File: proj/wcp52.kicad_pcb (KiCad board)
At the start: 4 copper layers, 100 x 100 mm, 301 parts, among them J1 MicroUSB-B, J2 IN1, J3 IN2, J4 OUT, J5 CONN-PJ-037A, J6 JLINK, J7 AUX, Q1 MMBT3906, Q10 MMBT3904, Q11 BFR540, Q12 BFR540, Q13 MMBT3904, Q14 MMBT3904, Q15 MMBT3904, Q16 MMBT3904, Q17 PZT2907A, Q18 PZT2907A, Q19 MMBT3904, Q2 IRLML6402, Q3 AOD417, Q4 MMBT3906, Q5 2N7002, Q6 2N7002, Q7 MMBT3906, Q8 2N7002, Q9 2N7002, U1 TL431AIDBZ, U10 MASWSS0162, U11 AD8310ARMZ, U12 ATSAM4S16CA-AU, U13 FT230XS_DNP, U14 L78M05CDT, U15 MC79M05CDT, U16 AZ1117CH-1.8TRG1, U17 MCP1700T-vv02E/TT, U2 LM393M, U3 LMH6714MF, U4 AD9958BCPZ, U5 LMH6714MF, U6 AD8000YRDZ, U7 THS3001IDGN, U8 MAADSS0008, U9 MASWSS0162, X1 25 MHz, X2 12MHz

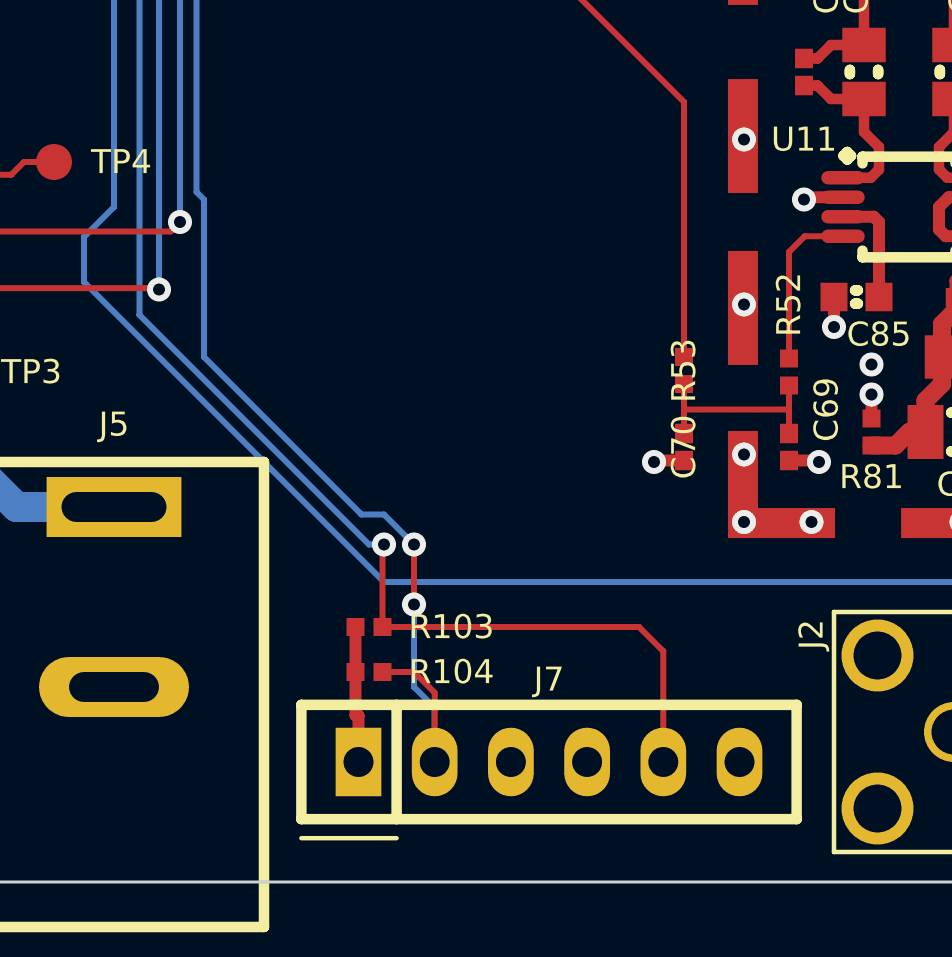
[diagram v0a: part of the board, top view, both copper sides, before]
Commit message: Add overload protection to aux power output
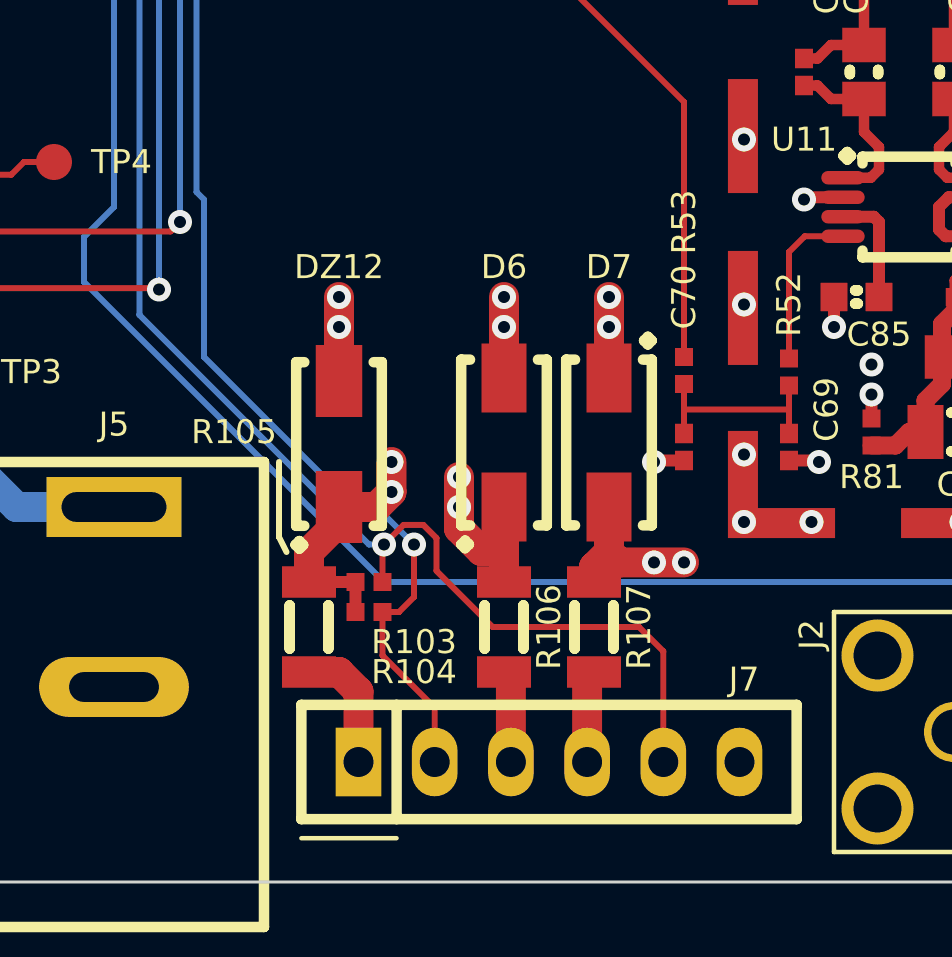
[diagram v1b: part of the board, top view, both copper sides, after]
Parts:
- added D6: S1A, IPC7351-Nominal:DIOM5326X292, F.Cu at (113.0, 110.3)
- added D7: S1A, IPC7351-Nominal:DIOM5326X292, F.Cu at (116.5, 110.3)
- added DZ12: 1SMA5914BT3G, IPC7351-Nominal:DIOM5226X203, F.Cu at (107.5, 110.4)
- added R105: 50mA, IPC7351-Nominal:RESC3216X60, F.Cu at (106.5, 116.5)
- added R106: 50mA, IPC7351-Nominal:RESC3216X60, F.Cu at (113.0, 116.5)
- added R107: 50mA, IPC7351-Nominal:RESC3216X60, F.Cu at (116.0, 116.5)
- moved R104 2.00 mm to (108.5, 116.0)
- moved R103 1.50 mm to (108.5, 115.0)
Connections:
- J7 pad 1: +3.3 -> Net-(J7-Pad1)
- J7 pad 3: +9 -> Net-(J7-Pad3)
- J7 pad 4: -9 -> Net-(J7-Pad4)
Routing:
- net GND: track 614.5 -> 622.7 mm, vias 241 -> 247
- net Net-(J7-Pad1): track 0.00 -> 4.27 mm
- net +3.3: track 112.8 -> 116.7 mm, vias 10 -> 12
- net +9: track 218.2 -> 222.1 mm, vias 8 -> 10
- net Net-(J7-Pad4): track 0.00 -> 3.48 mm
- net /MPU/I2C_SCL: track 61.1 -> 58.0 mm, vias 3 -> 2
- net Net-(J7-Pad3): track 0.00 -> 3.10 mm
- net /MPU/I2C_SDA: track 65.7 -> 66.4 mm
- net -9: track 276.4 -> 276.8 mm, vias 16 -> 18

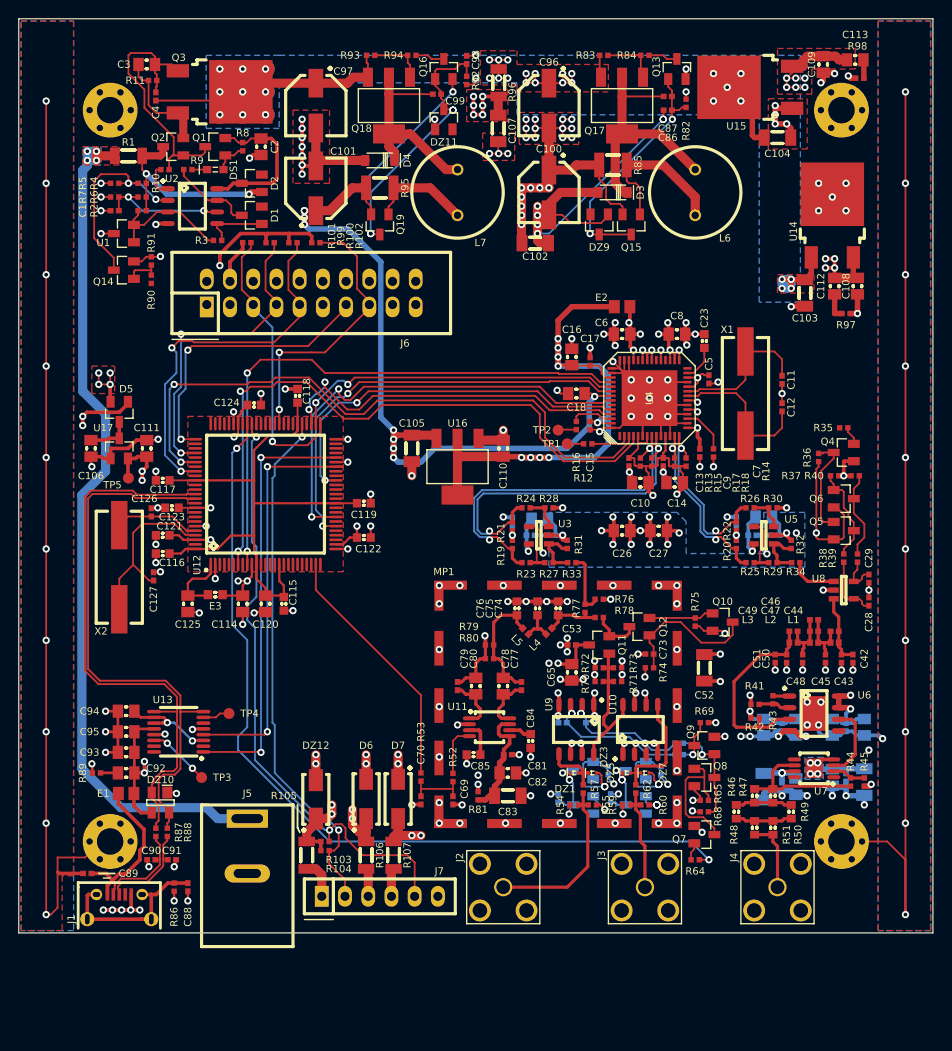
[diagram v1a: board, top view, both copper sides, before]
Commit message: Add some test points
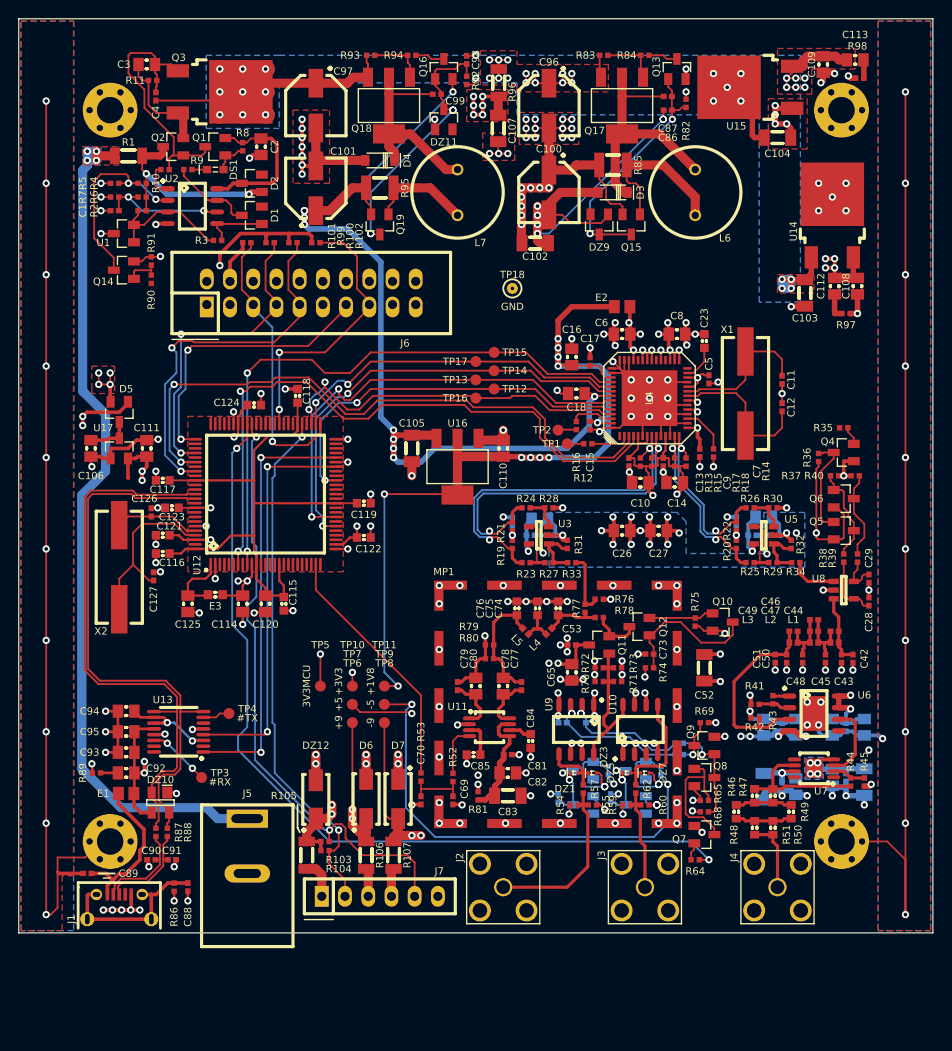
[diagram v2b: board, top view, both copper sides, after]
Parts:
- added TP10: +3V3, conn-test:TEST-SMD-SMALL, F.Cu at (111.5, 98.0)
- added TP11: +1V8, conn-test:TEST-SMD-SMALL, F.Cu at (115.0, 98.0)
- added TP12: MISO, conn-test:TEST-SMD-SMALL, F.Cu at (127.0, 65.5)
- added TP13: MOSI, conn-test:TEST-SMD-SMALL, F.Cu at (125.0, 64.5)
- added TP14: SCK, conn-test:TEST-SMD-SMALL, F.Cu at (127.0, 63.5)
- added TP15: IOUP, conn-test:TEST-SMD-SMALL, F.Cu at (127.0, 61.5)
- added TP16: SYNC, conn-test:TEST-SMD-SMALL, F.Cu at (125.0, 66.5)
- added TP17: #CS, conn-test:TEST-SMD-SMALL, F.Cu at (125.0, 62.5)
- added TP18: GND, conn-test:TEST-SMD-SMALL, F.Cu at (129.0, 54.5)
- added TP6: +9, conn-test:TEST-SMD-SMALL, F.Cu at (111.5, 102.0)
- added TP7: +5, conn-test:TEST-SMD-SMALL, F.Cu at (111.5, 100.0)
- added TP8: -9, conn-test:TEST-SMD-SMALL, F.Cu at (115.0, 102.0)
- added TP9: -5, conn-test:TEST-SMD-SMALL, F.Cu at (115.0, 100.0)
- moved TP5 31.0 mm to (108.0, 98.0)
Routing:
- net -5: track 215.6 -> 265.0 mm, vias 24 -> 25
- net +1.8: track 65.3 -> 96.4 mm, vias 9 -> 11
- net -9: track 276.8 -> 288.6 mm
- net +9: track 222.1 -> 231.6 mm
- net +5: track 277.8 -> 287.3 mm, vias 21 -> 22
- net +3.3SB: track 46.8 -> 50.3 mm, vias 10 -> 11
- net /Synth/IO_UPDATE: track 62.4 -> 64.3 mm
- net +3.3: track 116.7 -> 118.2 mm, vias 12 -> 13
- net /Synth/#CS: track 36.5 -> 38.0 mm
- net /Synth/SCLK: track 48.0 -> 49.0 mm
- net /Synth/SDI: track 50.0 -> 50.6 mm

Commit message: Tidy up F.Cu
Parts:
- added TP19: LEVEL, conn-test:TEST-SMD-SMALL, F.Cu at (115.0, 96.0)
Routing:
- net Net-(C127-Pad2): track 19.8 -> 22.8 mm
- net /Comm/USBPWR: track 21.7 -> 24.2 mm, vias 4 -> 6
- net -9: track 288.6 -> 290.2 mm
- net /MPU/ADIN: track 27.6 -> 29.2 mm
- net Net-(R2-Pad2): track 14.3 -> 15.6 mm
- net Net-(D1-Pad3): track 9.30 -> 10.5 mm
- net /Synth/IO_UPDATE: track 64.3 -> 63.1 mm
- net /MPU/TMS: track 34.8 -> 35.8 mm
- net /MPU/TDO: track 31.4 -> 32.3 mm
- net /MPU/#RST: track 30.5 -> 31.4 mm
- net /Synth/PWR_DWN_CTL: track 70.3 -> 69.6 mm
- net /Synth/MASTER_RESET: track 68.2 -> 67.7 mm
- added copper zone on F.Cu, net +1.8A
- added copper zone on F.Cu, net +3.3
- added copper zone on F.Cu, net /Comm/USBPWR

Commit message: Tidy up In1.Cu
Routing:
- net +5: track 287.3 -> 290.5 mm
- net +9: track 231.6 -> 230.4 mm
- net -9: track 290.2 -> 289.2 mm
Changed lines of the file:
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@@
     (thickness 1.6)
     (drawings 18)
-    (tracks 2882)
+    (tracks 2878)
     (zones 0)
     (modules 321)
@@
   (page A4)
   (layers
-    (0 F.Cu signal)
-    (1 In1.Cu signal hide)
+    (0 F.Cu signal hide)
+    (1 In1.Cu signal)
     (2 In2.Cu signal hide)
     (31 B.Cu signal hide)
@@
     (34 B.Paste user)
     (35 F.Paste user)
-    (36 B.SilkS user)
+    (36 B.SilkS user hide)
     (37 F.SilkS user hide)
     (38 B.Mask user)
     (39 F.Mask user)
-    (40 Dwgs.User user)
+    (40 Dwgs.User user hide)
     (41 Cmts.User user)
     (42 Eco1.User user)
@@
   )
   (setup
-    (last_trace_width 0.2)
+    (last_trace_width 1)
     (trace_clearance 0.152)
     (zone_clearance 0.2)
@@
     (mod_text_size 1 1)
     (mod_text_width 0.15)
-    (pad_size 1.2 1.2)
-    (pad_drill 0.4)
+    (pad_size 2 5)
+    (pad_drill 1)
     (pad_to_mask_clearance 0)
     (aux_axis_origin 0 0)
-    (visible_elements FFFE7F7F)
+    (visible_elements FFFC3E7F)
     (pcbplotparams
       (layerselection 0x00030_80000001)
@@
       (net 79 /PowerInput/IN))
     (pad 2 thru_hole oval (at 0 0 270) (size 2 5) (drill oval 1 3) (layers *.Cu *.Mask F.SilkS)
-      (net 1 GND))
+      (net 1 GND) (thermal_width 1.5))
     (model conn_misc/dc_socket.wrl
       (at (xyz 0 0 0))
@@
   (via (at 109.25 111) (size 0.8) (drill 0.4) (layers F.Cu B.Cu) (net 11))
   (segment (start 109.25 112) (end 109.25 111) (width 1) (layer F.Cu) (net 11))
+  (segment (start 85 63.75) (end 85 52) (width 0.2) (layer In1.Cu) (net 12))
+  (segment (start 85 52) (end 87 50) (width 0.2) (layer In1.Cu) (net 12))
+  (segment (start 87 50) (end 151.5 50) (width 0.2) (layer In1.Cu) (net 12))
+  (segment (start 151.5 50) (end 156.050001 54.550001) (width 0.2) (layer In1.Cu) (net 12))
+  (segment (start 156.050001 54.550001) (end 157.699999 54.550001) (width 0.2) (layer In1.Cu) (net 12))
   (segment (start 118 101) (end 120.5 101) (width 0.2) (layer In1.Cu) (net 12))
   (segment (start 111.5 100) (end 112.352001 100.852001) (width 0.2) (layer F.Cu) (net 12))
@@
   (segment (start 85 65) (end 85 66.85) (width 0.4) (layer F.Cu) (net 12))
   (segment (start 85 66.85) (end 85.05 66.9) (width 0.4) (layer F.Cu) (net 12))
-  (segment (start 85 63.75) (end 85 57.464962) (width 0.2) (layer In1.Cu) (net 12))
-  (segment (start 85 57.464962) (end 92.464962 50) (width 0.2) (layer In1.Cu) (net 12))
-  (segment (start 92.464962 50) (end 151.5 50) (width 0.2) (layer In1.Cu) (net 12))
-  (segment (start 151.5 50) (end 156.050001 54.550001) (width 0.2) (layer In1.Cu) (net 12))
-  (segment (start 156.050001 54.550001) (end 157.699999 54.550001) (width 0.2) (layer In1.Cu) (net 12))
   (segment (start 83.75 65) (end 83.75 63.75) (width 0.2) (layer F.Cu) (net 12))
   (via (at 83.75 63.75) (size 0.8) (drill 0.4) (layers F.Cu B.Cu) (net 12))
@@
   (segment (start 166.95 86.55) (end 166.35 86.55) (width 0.2) (layer F.Cu) (net 16))
   (segment (start 167.25 86.25) (end 166.95 86.55) (width 0.2) (layer F.Cu) (net 16))
+  (segment (start 173.5 104.5) (end 170.916189 107.083811) (width 1) (layer In1.Cu) (net 17))
+  (segment (start 163.584648 108.8) (end 158.48108 108.8) (width 1) (layer In1.Cu) (net 17))
+  (segment (start 170.916189 107.083811) (end 165.300837 107.083811) (width 1) (layer In1.Cu) (net 17))
+  (segment (start 165.300837 107.083811) (end 163.584648 108.8) (width 1) (layer In1.Cu) (net 17))
   (segment (start 111.5 102) (end 111.5 111.5) (width 0.2) (layer F.Cu) (net 17))
   (via (at 158.5 107.5) (size 0.8) (drill 0.4) (layers F.Cu B.Cu) (net 17))
@@
   (segment (start 158.5 107.5) (end 159.4 107.5) (width 0.6) (layer B.Cu) (net 17))
   (segment (start 158.5 108.55) (end 158.5 107.5) (width 0.6) (layer B.Cu) (net 17))
-  (segment (start 170.5 108.056962) (end 168.754961 109.802001) (width 1) (layer In1.Cu) (net 17))
-  (segment (start 170.5 107.5) (end 170.5 108.056962) (width 1) (layer In1.Cu) (net 17))
-  (segment (start 173.5 104.5) (end 170.5 107.5) (width 1) (layer In1.Cu) (net 17))
   (segment (start 170.75 89) (end 173.5 91.75) (width 1) (layer In1.Cu) (net 17))
   (segment (start 170.75 86.039302) (end 170.75 89) (width 1) (layer In1.Cu) (net 17))
@@
   (segment (start 166.350001 63.149999) (end 166.350001 81.639303) (width 1) (layer In1.Cu) (net 17))
   (segment (start 170.75 58.75) (end 166.350001 63.149999) (width 1) (layer In1.Cu) (net 17))
-  (segment (start 168.754961 109.802001) (end 166.858963 109.802001) (width 1) (layer In1.Cu) (net 17))
   (segment (start 170.75 29.75) (end 170.75 58.75) (width 1) (layer In1.Cu) (net 17))
   (segment (start 168 27) (end 170.75 29.75) (width 1) (layer In1.Cu) (net 17))
@@
   (segment (start 146.5 27) (end 168 27) (width 1) (layer In1.Cu) (net 17))
   (segment (start 140 33.5) (end 146.5 27) (width 1) (layer In1.Cu) (net 17))
-  (segment (start 166.858963 109.802001) (end 165.856962 108.8) (width 1) (layer In1.Cu) (net 17))
   (segment (start 125.75 33.5) (end 140 33.5) (width 1) (layer In1.Cu) (net 17))
   (segment (start 149.556968 115.75) (end 148.39982 115.75) (width 1) (layer In1.Cu) (net 17))
@@
   (segment (start 158.5 107.5) (end 158.5 108.78108) (width 1) (layer In1.Cu) (net 17))
   (segment (start 158.48108 108.8) (end 156.506968 108.8) (width 1) (layer In1.Cu) (net 17))
-  (segment (start 165.856962 108.8) (end 158.48108 108.8) (width 1) (layer In1.Cu) (net 17))
   (segment (start 123.42175 117.110248) (end 118.610248 117.110248) (width 1) (layer In1.Cu) (net 17))
   (segment (start 124.781998 115.75) (end 123.42175 117.110248) (width 0.4) (layer In1.Cu) (net 17))
@@
   (segment (start 112.246133 113.967669) (end 111.5 113.221536) (width 1) (layer F.Cu) (net 17))
   (segment (start 113 113.967669) (end 112.246133 113.967669) (width 1) (layer F.Cu) (net 17))
+  (segment (start 152.069541 33.680459) (end 157 28.75) (width 1) (layer In1.Cu) (net 18))
+  (segment (start 166.75 28.75) (end 169.5 31.5) (width 1) (layer In1.Cu) (net 18))
+  (segment (start 157 28.75) (end 166.75 28.75) (width 1) (layer In1.Cu) (net 18))
+  (segment (start 169.5 31.5) (end 169.5 57.5) (width 1) (layer In1.Cu) (net 18))
+  (segment (start 169.5 57.5) (end 164 63) (width 1) (layer In1.Cu) (net 18))
+  (segment (start 170 105) (end 168 105) (width 1) (layer In1.Cu) (net 18))
+  (segment (start 164 63) (end 164 81.477932) (width 1) (layer In1.Cu) (net 18))
+  (segment (start 164 81.477932) (end 169.5 86.977932) (width 1) (layer In1.Cu) (net 18))
+  (segment (start 169.5 86.977932) (end 169.5 90) (width 1) (layer In1.Cu) (net 18))
+  (segment (start 169.5 90) (end 170.75 91.25) (width 1) (layer In1.Cu) (net 18))
+  (segment (start 170.75 91.25) (end 170.75 104.25) (width 1) (layer In1.Cu) (net 18))
+  (segment (start 170.75 104.25) (end 170 105) (width 1) (layer In1.Cu) (net 18))
   (segment (start 131.75 45.5) (end 132.05 45.5) (width 1) (layer F.Cu) (net 18))
   (segment (start 132.05 45.5) (end 133 46.45) (width 1) (layer F.Cu) (net 18))
@@
   (segment (start 149.350001 112.899999) (end 148.610027 112.899999) (width 1) (layer In1.Cu) (net 18))
   (segment (start 162.4 105) (end 157.25 105) (width 1) (layer In1.Cu) (net 18))
-  (segment (start 152.069541 33.680459) (end 157 28.75) (width 1) (layer In1.Cu) (net 18))
-  (segment (start 157 28.75) (end 166.75 28.75) (width 1) (layer In1.Cu) (net 18))
-  (segment (start 166.75 28.75) (end 169.5 31.5) (width 1) (layer In1.Cu) (net 18))
-  (segment (start 169.5 31.5) (end 169.5 57.5) (width 1) (layer In1.Cu) (net 18))
-  (segment (start 169.5 57.5) (end 164 63) (width 1) (layer In1.Cu) (net 18))
-  (segment (start 164 63) (end 164 83.25) (width 1) (layer In1.Cu) (net 18))
-  (segment (start 164 83.25) (end 166.75 86) (width 1) (layer In1.Cu) (net 18))
-  (segment (start 166.75 86) (end 168.522068 86) (width 1) (layer In1.Cu) (net 18))
-  (segment (start 168.522068 86) (end 169.5 86.977932) (width 1) (layer In1.Cu) (net 18))
-  (segment (start 169.5 86.977932) (end 169.5 90) (width 1) (layer In1.Cu) (net 18))
-  (segment (start 169.5 90) (end 170.75 91.25) (width 1) (layer In1.Cu) (net 18))
-  (segment (start 170.75 91.25) (end 170.75 104.25) (width 1) (layer In1.Cu) (net 18))
-  (segment (start 170.75 104.25) (end 170 105) (width 1) (layer In1.Cu) (net 18))
-  (segment (start 170 105) (end 168 105) (width 1) (layer In1.Cu) (net 18))
   (via (at 168 105) (size 0.8) (drill 0.4) (layers F.Cu B.Cu) (net 18))
   (segment (start 168 105) (end 162.4 105) (width 1) (layer In1.Cu) (net 18))
@@
       (pts
         (xy 154 84) (xy 151 84) (xy 148 81) (xy 148 79) (xy 147 78)
-        (xy 130 78) (xy 130 83) (xy 123 83) (xy 123 75) (xy 140 75)
-        (xy 140 57.5) (xy 140 55.5) (xy 154 55.5) (xy 154 57.5) (xy 154 84)
+        (xy 130 78) (xy 130 85.5) (xy 120 85.5) (xy 120 75) (xy 141 75)
+        (xy 141 57.5) (xy 141 55.5) (xy 154 55.5) (xy 154 57.5) (xy 154 84)
       )
     )
@@
         (xy 147.5 81.5) (xy 150.5 84.5) (xy 154.5 84.5) (xy 154.5 55) (xy 133 55)
         (xy 133 50.5) (xy 91 50.5) (xy 91 54.5) (xy 85.5 54.5) (xy 85.5 66)
-        (xy 83 66) (xy 83 48.5) (xy 129 48.5) (xy 129 49.5) (xy 154 49.5)
-        (xy 154 50) (xy 154.5 50) (xy 165 50) (xy 165 53.5) (xy 159 59.5)
-        (xy 159 84) (xy 167 92) (xy 167 101.5)
+        (xy 83 66) (xy 83 48.5) (xy 129 48.5) (xy 129 49.5) (xy 132.5 49.5)
+        (xy 132.5 45.5) (xy 141.5 45.5) (xy 151.5 35.5) (xy 154 35.5) (xy 154 50)
+        (xy 154.5 50) (xy 165 50) (xy 165 53.5) (xy 159 59.5) (xy 159 84)
+        (xy 167 92) (xy 167 101.5)
       )
     )
@@
     (polygon
       (pts
-        (xy 129 74.5) (xy 139.5 74.5) (xy 139.5 55.5) (xy 133 55.5) (xy 133 64.5)
+        (xy 129 74.5) (xy 140.5 74.5) (xy 140.5 55.5) (xy 133 55.5) (xy 133 64.5)
         (xy 139 64.5) (xy 139 68) (xy 139 68.5) (xy 138 68.5) (xy 138 72)
         (xy 129 72)

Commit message: Add more 3D models
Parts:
- moved C30 4.81 mm to (163.2, 97.8), turned to 180 degrees
- moved C34 4.78 mm to (167.0, 97.8), turned to 0 degrees
- moved C32 1.80 mm to (164.5, 101.0), turned to 180 degrees
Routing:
- net +1.8: track 96.1 -> 68.2 mm
- net +3.3: track 118.2 -> 91.4 mm
- net +5: track 290.5 -> 289.3 mm
- net /MPU/CHANSEL: track 95.0 -> 94.2 mm
- net GND: track 622.4 -> 622.6 mm, vias 247 -> 246
